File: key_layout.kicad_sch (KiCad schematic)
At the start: 25 parts

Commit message: Savepoint!
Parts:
- added D10, D11, D12, D13, D14, D15, D16, D17, D18, D19, D2, D20, D21, D22, D23, D24, D25, D26, D3, D4, D5, D6, D7, D8, D9: 1N914, Diode_SMD:D_SOD-123, symbol Diode:1N914
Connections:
- net COL_3: now reaches S13.1
- net COL_3: now also S18.1, S23.1, S3.1, S8.1, D12.1 (K), D13.1 (K), D14.1 (K), D15.1 (K), D16.1 (K)
- net COL_1: now reaches S1.1, S11.1, S16.1, S21.1, S6.1
- net COL_1: now also D2.1 (K), D3.1 (K), D4.1 (K), D5.1 (K), D6.1 (K)
- net COL_2: now reaches S22.1
- net COL_2: now also S12.1, S17.1, S2.1, S7.1, D10.1 (K), D11.1 (K), D7.1 (K), D8.1 (K), D9.1 (K)
- net COL_4: now reaches S14.1
- net COL_4: now also S19.1, S24.1, S4.1, S9.1, D17.1 (K), D18.1 (K), D19.1 (K), D20.1 (K), D21.1 (K)
- net COL_5: now reaches S5.1
- net COL_5: now also S10.1, S15.1, S20.1, S25.1, D22.1 (K), D23.1 (K), D24.1 (K), D25.1 (K), D26.1 (K)
- new net: D14.2 (A), S13.2
- new net: D24.2 (A), S23.2
- new net: D18.2 (A), S17.2
- new net: D2.2 (A), S1.2
- new net: D23.2 (A), S22.2
- new net: D15.2 (A), S14.2
- new net: D5.2 (A), S4.2
- new net: D22.2 (A), S21.2
- new net: D6.2 (A), S5.2
- new net: D16.2 (A), S15.2
- new net: D9.2 (A), S8.2
- new net: D13.2 (A), S12.2
- new net: D17.2 (A), S16.2
- new net: D12.2 (A), S11.2
- new net: D25.2 (A), S24.2
- new net: D4.2 (A), S3.2
- new net: D7.2 (A), S6.2
- new net: D19.2 (A), S18.2
- new net: D20.2 (A), S19.2
- new net: D3.2 (A), S2.2
- new net: D11.2 (A), S10.2
- new net: D26.2 (A), S25.2
- new net: D8.2 (A), S7.2
- new net: D10.2 (A), S9.2
- new net: D21.2 (A), S20.2
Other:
- moved on the sheet: S10, S11, S12, S13, S14, S15, S16, S17, S18, S19, S20, S21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

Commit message: Savepoint!
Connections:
- net COL_1: no longer D2.1 (K), D3.1 (K), D4.1 (K), D5.1 (K), D6.1 (K)
- net COL_2: no longer D10.1 (K), D11.1 (K), D7.1 (K), D8.1 (K), D9.1 (K)
- net COL_3: no longer D12.1 (K), D13.1 (K), D14.1 (K), D15.1 (K), D16.1 (K)
- net COL_4: no longer D17.1 (K), D18.1 (K), D19.1 (K), D20.1 (K), D21.1 (K)
- net COL_5: no longer D22.1 (K), D23.1 (K), D24.1 (K), D25.1 (K), D26.1 (K)
- new net ROW_1: D2.1 (K), D3.1 (K), D4.1 (K), D5.1 (K), D6.1 (K)
- new net ROW_2: D10.1 (K), D11.1 (K), D7.1 (K), D8.1 (K), D9.1 (K)
- new net ROW_3: D12.1 (K), D13.1 (K), D14.1 (K), D15.1 (K), D16.1 (K)
- new net ROW_4: D17.1 (K), D18.1 (K), D19.1 (K), D20.1 (K), D21.1 (K)
- new net ROW_5: D22.1 (K), D23.1 (K), D24.1 (K), D25.1 (K), D26.1 (K)
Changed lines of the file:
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@@
 		)
 	)
-	(global_label "COL_2"
+	(global_label "ROW_2"
 		(shape input)
 		(at 120.65 102.87 0)
@@
 		)
 		(property "Intersheetrefs" "${INTERSHEET_REFS}"
-			(at 129.4409 102.87 0)
+			(at 129.8642 102.87 0)
 			(hide yes)
 			(show_name no)
@@
 		)
 	)
-	(global_label "COL_5"
+	(global_label "ROW_5"
 		(shape input)
 		(at 120.65 167.64 0)
@@
 		)
 		(property "Intersheetrefs" "${INTERSHEET_REFS}"
-			(at 129.4409 167.64 0)
+			(at 129.8642 167.64 0)
 			(hide yes)
 			(show_name no)
@@
 		)
 	)
-	(global_label "COL_1"
+	(global_label "ROW_1"
 		(shape input)
 		(at 120.65 82.55 0)
@@
 		)
 		(property "Intersheetrefs" "${INTERSHEET_REFS}"
-			(at 129.4409 82.55 0)
+			(at 129.8642 82.55 0)
 			(hide yes)
 			(show_name no)
@@
 		)
 	)
-	(global_label "COL_4"
+	(global_label "ROW_4"
 		(shape input)
 		(at 120.65 146.05 0)
@@
 		)
 		(property "Intersheetrefs" "${INTERSHEET_REFS}"
-			(at 129.4409 146.05 0)
+			(at 129.8642 146.05 0)
 			(hide yes)
 			(show_name no)
@@
 		)
 	)
-	(global_label "COL_3"
+	(global_label "ROW_3"
 		(shape input)
 		(at 120.65 124.46 0)
@@
 		)
 		(property "Intersheetrefs" "${INTERSHEET_REFS}"
-			(at 129.4409 124.46 0)
+			(at 129.8642 124.46 0)
 			(hide yes)
 			(show_name no)

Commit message: Savepoint!
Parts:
- removed D22, D23, D24, D25, D26: 1N914, Diode_SMD:D_SOD-123, symbol Diode:1N914
- removed S21, S22, S23, S24, S25: Keyswitch, symbol ScottoKeebs:Placeholder_Keyswitch
- S1, S10, S11, S12, S13, S14, S15, S16, S17, S18, S19, S2, S20, S3, S4, S5, S6, S7, S8, S9: footprint (none) -> ScottoKeebs_Hotswap:Hotswap_Choc_V1V2_1.00u
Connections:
- net ROW_3 is gone; now on net ROW_1: D12.1 (K), D13.1 (K), D14.1 (K), D15.1 (K), D16.1 (K)
- net ROW_4 is gone; now on net ROW_2: D17.1 (K), D18.1 (K), D19.1 (K), D20.1 (K), D21.1 (K)
- net COL_1: no longer S11.1, S16.1
- net COL_2: no longer S12.1, S17.1
- net COL_3: no longer S13.1, S18.1
- net COL_4: no longer S14.1, S19.1
- net COL_5: no longer S15.1, S20.1
- new net COL_10: S15.1, S20.1
- new net COL_6: S11.1, S16.1
- new net COL_7: S12.1, S17.1
- new net COL_8: S13.1, S18.1
- new net COL_9: S14.1, S19.1

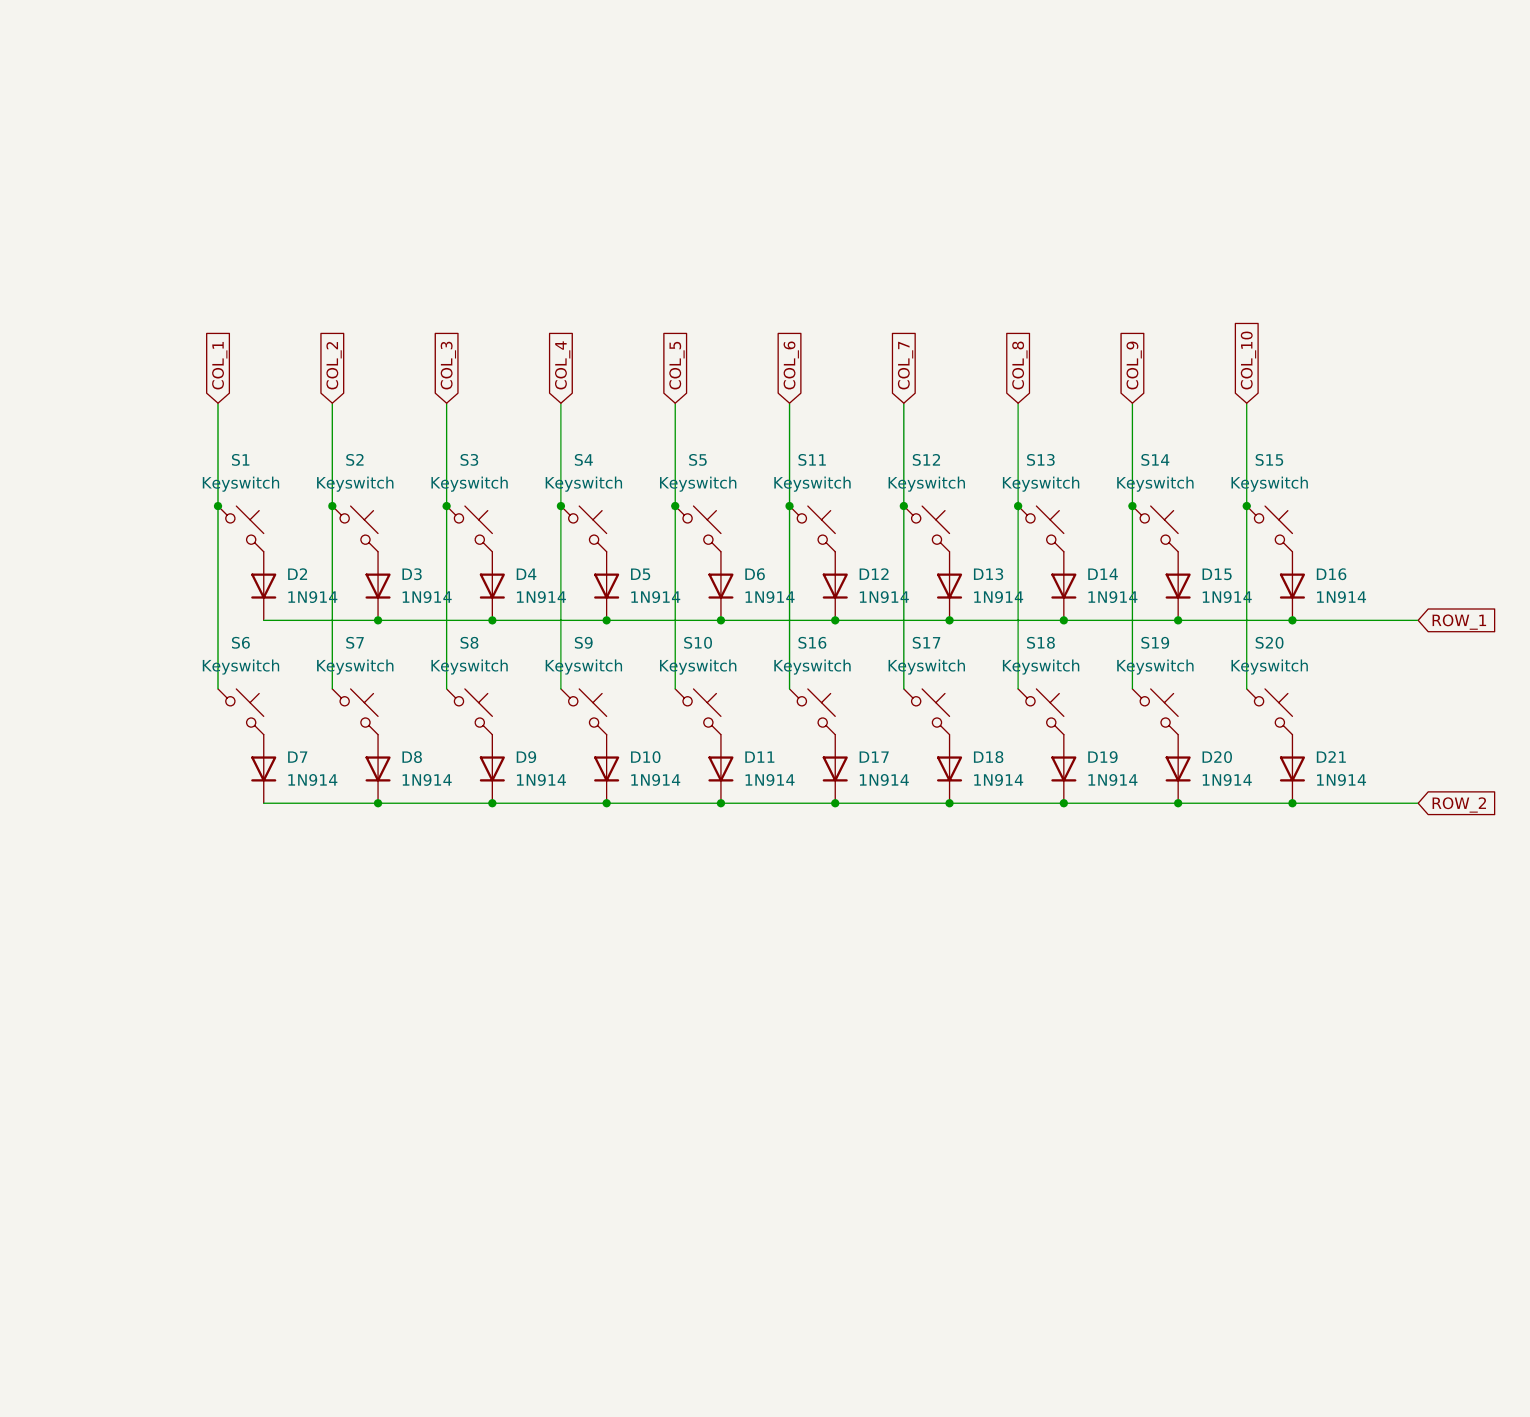
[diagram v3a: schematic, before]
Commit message: Smalled Caps and Restarting Layout.
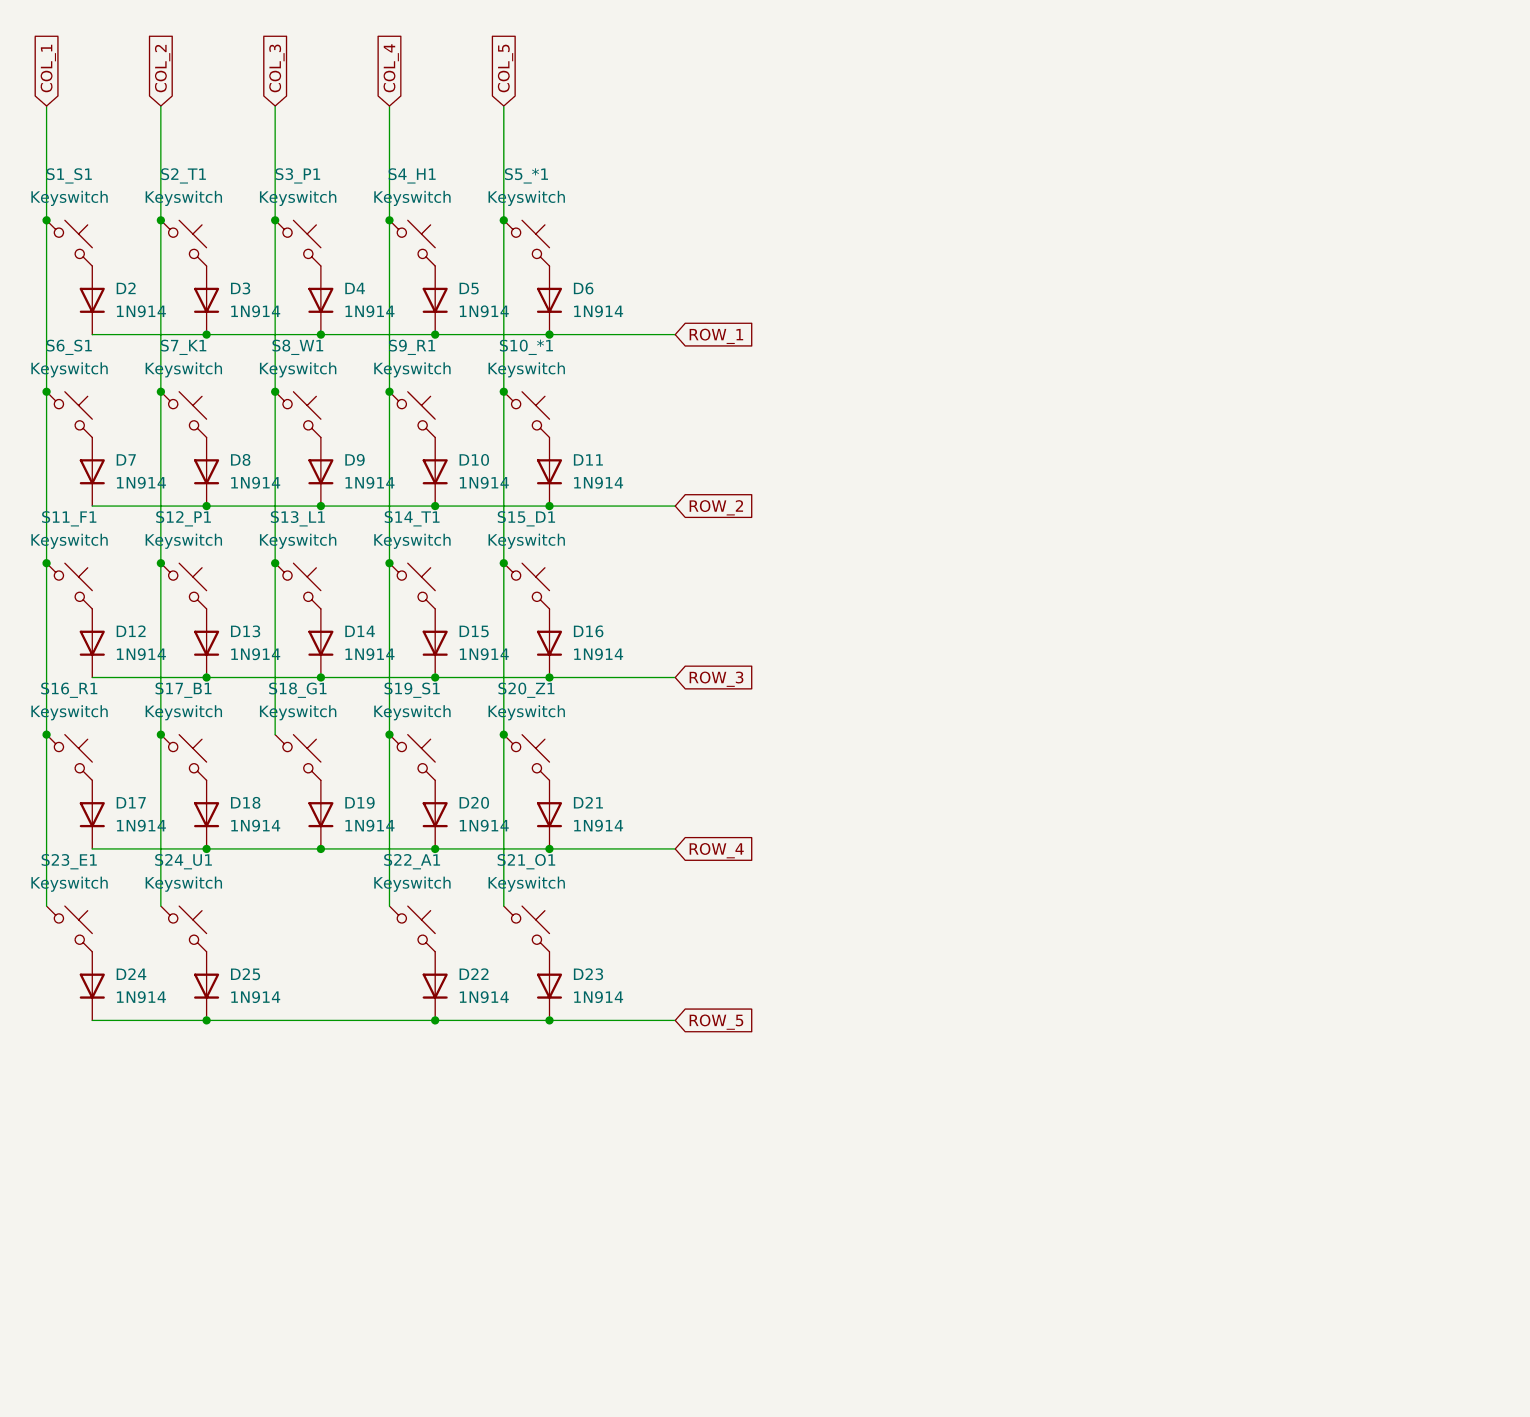
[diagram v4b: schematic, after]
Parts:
- removed S1, S10, S11, S12, S13, S14, S15, S16, S17, S18, S19, S2, S20, S3, S4, S5, S6, S7, S8, S9: Keyswitch, ScottoKeebs_Hotswap:Hotswap_Choc_V1V2_1.00u, symbol ScottoKeebs:Placeholder_Keyswitch
- added D22, D23, D24, D25: 1N914, Diode_SMD:D_SOD-123, symbol Diode:1N914
- added S10_*1, S11_F1, S12_P1, S13_L1, S14_T1, S15_D1, S16_R1, S17_B1, S18_G1, S19_S1, S1_S1, S20_Z1, S21_O1, S22_A1, S23_E1, S24_U1, S2_T1, S3_P1, S4_H1, S5_*1, S6_S1, S7_K1, S8_W1, S9_R1: Keyswitch, ScottoKeebs_Hotswap:Hotswap_Choc_V1V2_1.00u, symbol ScottoKeebs:Placeholder_Keyswitch
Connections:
- net COL_1: now also S11_F1.1, S16_R1.1, S1_S1.1, S23_E1.1, S6_S1.1
- net COL_2: now also S12_P1.1, S17_B1.1, S24_U1.1, S2_T1.1, S7_K1.1
- net COL_3: now also S13_L1.1, S18_G1.1, S3_P1.1, S8_W1.1
- net COL_4: now also S14_T1.1, S19_S1.1, S22_A1.1, S4_H1.1, S9_R1.1
- net COL_5: now also S10_*1.1, S15_D1.1, S20_Z1.1, S21_O1.1, S5_*1.1
- net ROW_1: no longer D12.1 (K), D13.1 (K), D14.1 (K), D15.1 (K), D16.1 (K)
- net ROW_2: no longer D17.1 (K), D18.1 (K), D19.1 (K), D20.1 (K), D21.1 (K)
- net at D21.2 (A): now also S20_Z1.2
- net at D2.2 (A): now also S1_S1.2
- net at D13.2 (A): now also S12_P1.2
- net at D5.2 (A): now also S4_H1.2
- net at D19.2 (A): now also S18_G1.2
- net at D6.2 (A): now also S5_*1.2
- net at D9.2 (A): now also S8_W1.2
- net at D16.2 (A): now also S15_D1.2
- net at D14.2 (A): now also S13_L1.2
- net at D18.2 (A): now also S17_B1.2
- net at D4.2 (A): now also S3_P1.2
- net at D17.2 (A): now also S16_R1.2
- net at D15.2 (A): now also S14_T1.2
- net at D7.2 (A): now also S6_S1.2
- net at D12.2 (A): now also S11_F1.2
- net at D3.2 (A): now also S2_T1.2
- net at D20.2 (A): now also S19_S1.2
- net at D11.2 (A): now also S10_*1.2
- net at D8.2 (A): now also S7_K1.2
- net at D10.2 (A): now also S9_R1.2
- new net: D25.2 (A), S24_U1.2
- new net: D23.2 (A), S21_O1.2
- new net: D24.2 (A), S23_E1.2
- new net: D22.2 (A), S22_A1.2
- new net ROW_3: D12.1 (K), D13.1 (K), D14.1 (K), D15.1 (K), D16.1 (K)
- new net ROW_4: D17.1 (K), D18.1 (K), D19.1 (K), D20.1 (K), D21.1 (K)
- new net ROW_5: D22.1 (K), D23.1 (K), D24.1 (K), D25.1 (K)

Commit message: Layout changes & wiring testing
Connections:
- net COL_1: no longer S23_E1.1
- net COL_3: now also S23_E1.1
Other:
- moved on the sheet: D24, S23_E1
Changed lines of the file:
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@@
 	)
 	(junction
-		(at 57.15 57.15)
+		(at 74.93 127)
 		(diameter 0)
 		(color 0 0 0 0)
 	)
 	(junction
-		(at 44.45 95.25)
+		(at 57.15 57.15)
 		(diameter 0)
 		(color 0 0 0 0)
@@
 	)
 	(junction
-		(at 74.93 127)
+		(at 62.23 127)
 		(diameter 0)
 		(color 0 0 0 0)
@@
 	)
 	(junction
-		(at 31.75 95.25)
+		(at 74.93 69.85)
 		(diameter 0)
 		(color 0 0 0 0)
 	)
 	(junction
-		(at 74.93 69.85)
+		(at 82.55 57.15)
 		(diameter 0)
 		(color 0 0 0 0)
 	)
 	(junction
-		(at 82.55 57.15)
+		(at 57.15 95.25)
 		(diameter 0)
 		(color 0 0 0 0)
@@
 	)
 	(junction
-		(at 49.53 127)
+		(at 44.45 95.25)
 		(diameter 0)
 		(color 0 0 0 0)
@@
 	(wire
 		(pts
-			(xy 44.45 95.25) (xy 44.45 114.3)
-		)
-		(stroke
-			(width 0)
-			(type default)
-		)
-	)
-	(wire
-		(pts
 			(xy 69.85 57.15) (xy 69.85 76.2)
 		)
@@
 	(wire
 		(pts
-			(xy 31.75 95.25) (xy 31.75 114.3)
-		)
-		(stroke
-			(width 0)
-			(type default)
-		)
-	)
-	(wire
-		(pts
 			(xy 69.85 95.25) (xy 69.85 114.3)
 		)
@@
 	(wire
 		(pts
-			(xy 36.83 127) (xy 49.53 127)
-		)
-		(stroke
-			(width 0)
-			(type default)
-		)
-	)
-	(wire
-		(pts
 			(xy 36.83 69.85) (xy 49.53 69.85)
 		)
@@
 	(wire
 		(pts
-			(xy 49.53 127) (xy 74.93 127)
+			(xy 44.45 25.4) (xy 44.45 38.1)
 		)
 		(stroke
@@
 	(wire
 		(pts
-			(xy 44.45 25.4) (xy 44.45 38.1)
+			(xy 31.75 38.1) (xy 31.75 57.15)
 		)
 		(stroke
@@
 	(wire
 		(pts
-			(xy 31.75 38.1) (xy 31.75 57.15)
+			(xy 69.85 38.1) (xy 69.85 57.15)
 		)
 		(stroke
@@
 	(wire
 		(pts
-			(xy 69.85 38.1) (xy 69.85 57.15)
+			(xy 57.15 114.3) (xy 57.15 95.25)
 		)
 		(stroke
@@
 	(wire
 		(pts
+			(xy 49.53 127) (xy 62.23 127)
+		)
+		(stroke
+			(width 0)
+			(type default)
+		)
+	)
+	(wire
+		(pts
 			(xy 31.75 57.15) (xy 31.75 76.2)
 		)
@@
 	(wire
 		(pts
+			(xy 62.23 127) (xy 74.93 127)
+		)
+		(stroke
+			(width 0)
+			(type default)
+		)
+	)
+	(wire
+		(pts
 			(xy 62.23 69.85) (xy 74.93 69.85)
 		)
@@
 	(wire
 		(pts
+			(xy 44.45 114.3) (xy 44.45 95.25)
+		)
+		(stroke
+			(width 0)
+			(type default)
+		)
+	)
+	(wire
+		(pts
 			(xy 69.85 25.4) (xy 69.85 38.1)
 		)
@@
 	(symbol
 		(lib_id "ScottoKeebs:Placeholder_Keyswitch")
-		(at 34.29 116.84 0)
+		(at 59.69 116.84 0)
 		(unit 1)
 		(body_style 1)
@@
 		(fields_autoplaced yes)
 		(property "Reference" "S23_E1"
-			(at 34.29 109.22 0)
+			(at 59.69 109.22 0)
 			(show_name no)
 			(do_not_autoplace no)
@@
 		)
 		(property "Value" "Keyswitch"
-			(at 34.29 111.76 0)
+			(at 59.69 111.76 0)
 			(show_name no)
 			(do_not_autoplace no)
@@
 		)
 		(property "Footprint" "ScottoKeebs_Hotswap:Hotswap_Choc_V1V2_1.00u"
-			(at 34.29 116.84 0)
+			(at 59.69 116.84 0)
 			(hide yes)
 			(show_name no)
@@
 		)
 		(property "Datasheet" ""
-			(at 34.29 116.84 0)
+			(at 59.69 116.84 0)
 			(hide yes)
 			(show_name no)
@@
 		)
 		(property "Description" "Push button switch, normally open, two pins, 45° tilted"
-			(at 34.29 116.84 0)
+			(at 59.69 116.84 0)
 			(hide yes)
 			(show_name no)
@@
 	(symbol
 		(lib_id "Diode:1N914")
-		(at 36.83 123.19 90)
+		(at 62.23 123.19 90)
 		(unit 1)
 		(body_style 1)
@@
 		(fields_autoplaced yes)
 		(property "Reference" "D24"
-			(at 39.37 121.9199 90)
+			(at 64.77 121.9199 90)
 			(show_name no)
 			(do_not_autoplace no)
@@
 		)
 		(property "Value" "1N914"
-			(at 39.37 124.4599 90)
+			(at 64.77 124.4599 90)
 			(show_name no)
 			(do_not_autoplace no)
@@
 		)
 		(property "Footprint" "Diode_SMD:D_SOD-123"
-			(at 41.275 123.19 0)
+			(at 66.675 123.19 0)
 			(hide yes)
 			(show_name no)
@@
 		)
 		(property "Datasheet" "http://www.vishay.com/docs/85622/1n914.pdf"
-			(at 36.83 123.19 0)
+			(at 62.23 123.19 0)
 			(hide yes)
 			(show_name no)
@@
 		)
 		(property "Description" "100V 0.3A Small Signal Fast Switching Diode, DO-35"
-			(at 36.83 123.19 0)
+			(at 62.23 123.19 0)
 			(hide yes)
 			(show_name no)
@@
 		)
 		(property "Sim.Device" "D"
-			(at 36.83 123.19 0)
+			(at 62.23 123.19 0)
 			(hide yes)
 			(show_name no)
@@
 		)
 		(property "Sim.Pins" "1=K 2=A"
-			(at 36.83 123.19 0)
+			(at 62.23 123.19 0)
 			(hide yes)
 			(show_name no)
